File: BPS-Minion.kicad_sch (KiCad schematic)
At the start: 138 parts, among them J1 TopConn, J10 TempConn2, J11 SOMConnector, J2 BottomConn, J3 Conn_01x24_Female, J3 DTENConfig, J4 IsoConfig, J5 IN, J6 OUT, J8 RegularSPIConn, J9 TempConn1, Q1 BSS308PE, Q10 BSS308PE, Q11 BSS308PE, Q12 BSS308PE, Q13 NSV1C201MZ4, Q2 BSS308PE, Q3 BSS308PE, Q4 BSS308PE, Q5 BSS308PE, Q6 BSS308PE, Q7 BSS308PE, Q8 BSS308PE, Q9 BSS308PE, SW1 Power Switch, U1 ADS7953SBDBT, U1 LTC6811-1, U2 HX1188FNL, U3 LM321, U3 LTC6255, U4 LTC1380, U5 LTC1380

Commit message: ADC Power all 3.3V
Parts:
- removed C1, C10, C11, C12, C2, C3, C4, C5, C6, C7, C8, C9: 10n, Capacitor_SMD:C_0805_2012Metric, symbol Device:C_Small
- removed C13, C20: 100n, Capacitor_SMD:C_0805_2012Metric, symbol Device:C_Small
- removed C14, C15, C16: 1u, Capacitor_SMD:C_0805_2012Metric, symbol Device:C_Small
- removed L1, L10, L11, L12, L2, L3, L4, L5, L6, L7, L8, L9: 600, Inductor_SMD:L_0805_2012Metric, symbol Device:Ferrite_Bead_Small
- removed Q1, Q10, Q11, Q12, Q2, Q3, Q4, Q5, Q6, Q7, Q8, Q9: BSS308PE, Package_TO_SOT_SMD:SOT-23, symbol Device:Q_PMOS_GSD
- removed Q13: NSV1C201MZ4, Package_TO_SOT_SMD:SOT-223, symbol Device:Q_NPN_BCEC
- removed R1, R10, R11, R12, R2, R3, R4, R5, R6, R7, R8, R9: 33R, Resistor_SMD:R_2512_6332Metric, symbol Device:R_Small
- removed R13, R14, R15, R16, R17, R18, R19, R20, R21, R22, R23, R24, R25: 100, Resistor_SMD:R_0805_2012Metric, symbol Device:R_Small
- removed R26: 100, Resistor_SMD:R_0805_2012Metric, symbol Device:R
- removed R27: 806, Resistor_SMD:R_0805_2012Metric, symbol Device:R_Small
- removed R28: 1.2k, Resistor_SMD:R_0805_2012Metric, symbol Device:R_Small
- removed SW1: Power Switch, Button_Switch_THT:SW_CuK_OS102011MA1QN1_SPDT_Angled, symbol Switch:SW_SPDT
- removed TP1: V+, TestPoint:TestPoint_Keystone_5005-5009_Compact, symbol Connector:TestPoint
- removed TP2: VREG, TestPoint:TestPoint_Keystone_5005-5009_Compact, symbol Connector:TestPoint
- removed TP3: V-, TestPoint:TestPoint_Keystone_5005-5009_Compact, symbol Connector:TestPoint
- removed U1: LTC6811-1, UTSVT_BPS:LTC6811HG-1-PBF, symbol utsvt-bps:LTC6811-1
- added U4: BQ7695201PFBR, Package_QFP:TQFP-48_7x7mm_P0.5mm, symbol utsvt-chips:BQ7695201PFBR
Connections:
- net +3.3V: now also U1.4 (REFP), U1.5 (VA+)
- net +5V: no longer U1.29 (VA+), U1.4 (REFP), U1.5 (VA+)
- net GND: no longer D12.1 (K)
- new net Batt0: D12.1 (K)
- new net LDO1: U1.29 (VA+)
- no-connect marks 13 -> 9
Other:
- note removed: "These Jumpers are for configuring the board to measure less than 12 cells"
- note removed: "These capacitors should have a voltage rating greater than 50V"
- moved on the sheet: U1

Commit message: bms chip started
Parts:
- removed C17: 10n, Capacitor_SMD:C_0805_2012Metric, symbol Device:C_Small
- removed C18, C19: 100n, Capacitor_SMD:C_0805_2012Metric, symbol Device:C_Small
- removed J10: TempConn2, Connector_PinHeader_2.54mm:PinHeader_1x10_P2.54mm_Vertical, symbol Connector_Generic:Conn_01x10
- removed J9: TempConn1, Connector_PinHeader_2.54mm:PinHeader_1x10_P2.54mm_Vertical, symbol Connector_Generic:Conn_01x10
- removed R43: 100, Resistor_SMD:R_0805_2012Metric, symbol Device:R_Small
- removed R44, R46: 4.7k, Resistor_SMD:R_0805_2012Metric, symbol Device:R_Small
- removed R47: 10k, Resistor_SMD:R_0805_2012Metric, symbol Device:R_Small
- removed U3: LTC6255, UTSVT_BPS:LTC6255CS6-TRMPBF, symbol utsvt-bps:LTC6255
- removed U4, U5: LTC1380, UTSVT_BPS:LTC1380CS-PBF, symbol utsvt-bps:LTC1380
- added C1, C10, C11, C12, C13, C14, C15, C16, C2, C3, C4, C5, C6, C7, C8, C9: 220nF, symbol Device:C
- added R1, R10, R11, R12, R13, R14, R15, R16, R2, R3, R4, R5, R6, R7, R8, R9: 20, symbol Device:R_US
- J1, J2: symbol Connector_Generic:Conn_01x07 -> Connector_Generic:Conn_01x08
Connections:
- net +3.3V: now also U3.5 (V+); no longer U1.4 (REFP)
- net +5V: no longer U3.5 (V+)
- net GND: now also U4.16 (VC0), C16.1; no longer U1.3 (REFM)
- net GNDA: now also U1.3 (REFM)
- net VDDA: now also U1.4 (REFP)
- net at J2.1 (Pin_1): now also R16.2
- net at J2.2 (Pin_2): now also R15.2
- net at J2.3 (Pin_3): now also R14.2
- net at J2.4 (Pin_4): now also R13.2
- net at J2.5 (Pin_5): now also R12.2
- net at J2.6 (Pin_6): now also R11.2
- net at J2.7 (Pin_7): now also R10.2
- net at J1.1 (Pin_1): now also R8.2
- net at J1.2 (Pin_2): now also R7.2
- net at J1.3 (Pin_3): now also R6.2
- net at J1.4 (Pin_4): now also R5.2
- net at J1.5 (Pin_5): now also R4.2
- net at J1.6 (Pin_6): now also R3.2
- net at J1.7 (Pin_7): now also R2.2
- net cell15: now reaches U4.1 (VC15)
- net cell15: now also C1.1, C2.2, R2.1
- net cell6: now reaches U4.10 (VC6)
- net cell6: now also C10.1, C11.2, R11.1
- net cell5: now reaches U4.11 (VC5)
- net cell5: now also C11.1, C12.2, R12.1
- net cell4: now reaches U4.12 (VC4)
- net cell4: now also C12.1, C13.2, R13.1
- net cell3: now reaches U4.13 (VC3)
- net cell3: now also C13.1, C14.2, R14.1
- net cell2: now reaches U4.14 (VC2)
- net cell2: now also C14.1, C15.2, R15.1
- net cell1: now reaches U4.15 (VC1)
- net cell1: now also C15.1, C16.2, R16.1
- net cell14: now reaches U4.2 (VC14)
- net cell14: now also C2.1, C3.2, R3.1
- net cell13: now reaches U4.3 (VC13)
- net cell13: now also C3.1, C4.2, R4.1
- net cell12: now reaches U4.4 (VC12)
- net cell12: now also C4.1, C5.2, R5.1
- net cell16: now reaches U4.48 (VC16)
- net cell16: now also C1.2, R1.1
- net cell11: now reaches U4.5 (VC11)
- net cell11: now also C5.1, C6.2, R6.1
- net cell10: now reaches U4.6 (VC10)
- net cell10: now also C6.1, C7.2, R7.1
- net cell9: now reaches U4.7 (VC9)
- net cell9: now also C7.1, C8.2, R8.1
- net cell8: now reaches U4.8 (VC8)
- net cell8: now also C8.1, C9.2, R9.1
- net cell7: now reaches U4.9 (VC7)
- net cell7: now also C10.2, C9.1, R10.1
- new net: J2.8 (Pin_8), R9.2
- new net: J1.8 (Pin_8), R1.2
- no-connect marks 9 -> 8
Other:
- moved on the sheet: C21, C22, FB17, FB18, J11, J3, R49, R50, U1, U3, U4

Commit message: BMS chip is fully wired
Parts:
- removed J5: IN, Connector_Molex:Molex_Micro-Fit_3.0_43650-0200_1x02_P3.00mm_Horizontal, symbol Connector_Generic:Conn_01x02
- removed J6: OUT, Connector_Molex:Molex_Micro-Fit_3.0_43650-0200_1x02_P3.00mm_Horizontal, symbol Connector_Generic:Conn_01x02
- removed J8: RegularSPIConn, Connector_PinHeader_2.54mm:PinHeader_1x05_P2.54mm_Vertical, symbol Connector_Generic:Conn_01x05
- removed R29, R30: 120, Resistor_SMD:R_0805_2012Metric, symbol Device:R_Small
- removed R48: 5.1k, Resistor_SMD:R_0805_2012Metric, symbol Device:R_Small
- removed U2: HX1188FNL, UTSVT_Passive:HXXXX, symbol utsvt-chips:HX1188FNL
- added C17: 220nF, symbol Device:C
- added C18: 4.7u, symbol Device:C
- added C19: 1u, symbol Device:C
- added C20: 100p, symbol Device:C
- added D14: D, symbol Device:D
- added J6: TopConn, Connector_Molex:Molex_Micro-Fit_3.0_43650-0700_1x07_P3.00mm_Horizontal, symbol Connector_Generic:Conn_01x06
- added R17: 20, symbol Device:R_US
- added R18, R19: 10k, symbol Device:R_US
- added R20: 100, symbol Device:R_US
- added TP1, TP10, TP11, TP12, TP13, TP14, TP15, TP2, TP3, TP4, TP5, TP6, TP7, TP8, TP9: TestPoint_2Pole, symbol Connector:TestPoint_2Pole
- J1, J2: symbol Connector_Generic:Conn_01x08 -> Connector_Generic:Conn_01x06
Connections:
- net GND: now also J2.1 (Pin_1), U4.17 (VSS), U4.18 (SRP), U4.20 (SRN), U4.36 (REGIN), U4.37 (BREG), C17.1, C18.1, C19.1, C20.1, R17.2; no longer U4.16 (VC0)
- net I2C1_SCL: now also U4.26 (SCL)
- net I2C1_SDA: now also U4.27 (SDA)
- net SPI2_MISO: now also U4.32 (DDSG)
- net SPI2_MOSI: now also U4.31 (DCHG)
- net SPI2_NSS: now also U4.33 (RST_SHUT)
- net SPI2_SCK: now also U4.38 (FUSE)
- net cell1: now also TP15.1
- net cell10: now also TP6.1, TP7.2
- net cell11: now also TP5.1, TP6.2
- net cell12: now also TP4.1, TP5.2
- net cell13: now also TP3.1, TP4.2
- net cell14: now also TP2.1, TP3.2
- net cell15: now also TP1.1, TP2.2
- net cell16: now also TP1.2
- net cell2: now also TP14.1, TP15.2
- net cell3: now also TP13.1, TP14.2
- net cell4: now also TP12.1, TP13.2
- net cell5: now also TP11.1, TP12.2
- net cell6: now also TP10.1, TP11.2
- net cell7: now also TP10.2, TP9.1
- net cell8: now also TP8.1, TP9.2
- net cell9: now also TP7.1, TP8.2
- net at R16.2: now also J2.2 (Pin_2); no longer J2.1 (Pin_1)
- net at R15.2: now also J2.3 (Pin_3); no longer J2.2 (Pin_2)
- net at R14.2: now also J2.4 (Pin_4); no longer J2.3 (Pin_3)
- net at R13.2: now also J2.5 (Pin_5); no longer J2.4 (Pin_4)
- net at R12.2: now also J2.6 (Pin_6); no longer J2.5 (Pin_5)
- net at R11.2: now also J1.1 (Pin_1); no longer J2.6 (Pin_6)
- net at R10.2: now also J1.2 (Pin_2); no longer J2.7 (Pin_7)
- net at R9.2: now also J1.3 (Pin_3); no longer J2.8 (Pin_8)
- net at R8.2: now also J1.4 (Pin_4); no longer J1.1 (Pin_1)
- net at R7.2: now also J1.5 (Pin_5); no longer J1.2 (Pin_2)
- net at R6.2: now also J1.6 (Pin_6); no longer J1.3 (Pin_3)
- net at R5.2: now also J6.1 (Pin_1); no longer J1.4 (Pin_4)
- net at R4.2: now also J6.2 (Pin_2); no longer J1.5 (Pin_5)
- net at R3.2: now also J6.3 (Pin_3); no longer J1.6 (Pin_6)
- net at R2.2: now also J6.4 (Pin_4); no longer J1.7 (Pin_7)
- net PACK+: now reaches R1.2
- net PACK+: now also D14.2 (A), J6.5 (Pin_5), R18.1, R19.1; no longer J1.8 (Pin_8)
- net at U4.24 (REG18): now also C18.2
- net at U4.41 (LD): now also R19.2
- net at U4.42 (PACK): now also R18.2
- net at U4.46 (CP1): now also U4.47 (BAT), C19.2, C20.2, R20.1
- new net: D14.1 (K), R20.2
- new net cell0: C17.2, R17.1, U4.16 (VC0)
- no-connect marks 8 -> 17
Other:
- note removed: "SDO is an open-drain output so a pull-up resistor is required for regular SPI."
- moved on the sheet: C1, C10, C11, C12, C13, C14, C15, C16, C2, C3, C4, C5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

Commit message: clean up
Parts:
- removed D1, D10, D11, D12, D2, D3, D4, D5, D6, D7, D8, D9: Red, LED_SMD:LED_0805_2012Metric, symbol Device:LED
- removed J3: DTENConfig, Connector_PinHeader_2.54mm:PinHeader_1x03_P2.54mm_Vertical, symbol Connector_Generic:Conn_01x03
- removed J4: IsoConfig, Connector_PinHeader_2.54mm:PinHeader_1x03_P2.54mm_Vertical, symbol Connector_Generic:Conn_01x03
- removed R31, R32, R33, R34, R35, R36, R37, R38, R39, R40, R41, R42: 1.2k, Resistor_SMD:R_0805_2012Metric, symbol Device:R
- removed R45: 1.5k, Resistor_SMD:R_0805_2012Metric, symbol Device:R
- added C23, C25: 4.7u, symbol Device:C
- added C24: 1u, symbol Device:C
- added C26: .47u, symbol Device:C
- added R21: 1k, symbol Device:R_US
- added U2: REF35160QDBVR, Package_SO:TSOP-6_1.65x3.05mm_P0.95mm, symbol utsvt-power-regulators:REF35160QDBVR
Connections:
- net LDO1 is gone; now on net VDDA: U1.29 (VA+)
- net +3.3V: no longer U1.5 (VA+)
- net +5V: now also R21.2
- net GND: no longer U1.19 (AGND), U1.20 (AGND)
- net GNDA: now also U1.19 (AGND), U1.20 (AGND), C23.1, C24.2, C25.2, U2.1 (GND), U2.2 (GND)
- net VDDA: now also U1.5 (VA+), C23.2, U2.3 (EN), U2.4 (VIN); no longer U1.4 (REFP)
- net at D13.2 (A): now also R21.1
- net at C19.2, C20.2, R20.1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: now also C26.2; no longer U4.46 (CP1)
- new net: C26.1, U4.46 (CP1)
- new net: C24.1, U2.5 (NR)
- new net 2V5_Ref: C25.1, U1.4 (REFP), U2.6 (VREF)
- no-connect marks 17 -> 21
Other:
- note added: "BMS"
- note added: "SOM Connection Input"
- note added: "Temp Sensor Connector"
- note added: "Temperature ADC and Filter"
- moved on the sheet: C18, C19, C20, C21, C22, D13, D14, FB17, FB18, J11, J3, MH1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

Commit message: edited some mistakes out
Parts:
- removed D14: D, symbol Device:D
- added D1: BAS16W, Package_TO_SOT_SMD:SOT-323_SC-70, symbol Diode:BAS16W
- C1, C10, C11, C12, C13, C14, C15, C16, C17, C18, C19, C2, C20, C23, C24, C25, C26, C3, C4, C5, C6, C7, C8, C9: footprint (none) -> Capacitor_SMD:C_0805_2012Metric_Pad1.18x1.45mm_HandSolder
- C21, C22: value C -> 47n; footprint (none) -> Capacitor_SMD:C_0805_2012Metric_Pad1.18x1.45mm_HandSolder
- R1, R10, R11, R12, R13, R14, R15, R16, R17, R18, R19, R2, R20, R21, R3, R4, R5, R6, R7, R8, R9: footprint (none) -> Resistor_SMD:R_0805_2012Metric_Pad1.20x1.40mm_HandSolder
- R49, R50: value R_US -> 4.7k; footprint (none) -> Resistor_SMD:R_0805_2012Metric_Pad1.20x1.40mm_HandSolder
- TP1, TP10, TP11, TP12, TP13, TP14, TP15, TP2, TP3, TP4, TP5, TP6, TP7, TP8, TP9: footprint (none) -> Jumper:SolderJumper-2_P1.3mm_Open_RoundedPad1.0x1.5mm
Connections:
- net PACK+: now also D1.1 (A)
- net at R20.2: now also D1.3 (K)
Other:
- moved on the sheet: R20

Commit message: new sheets
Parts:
- removed C1, C10, C11, C12, C13, C14, C15, C16, C17, C2, C3, C4, C5, C6, C7, C8, C9: 220nF, Capacitor_SMD:C_0805_2012Metric_Pad1.18x1.45mm_HandSolder, symbol Device:C
- removed C18, C23, C25: 4.7u, Capacitor_SMD:C_0805_2012Metric_Pad1.18x1.45mm_HandSolder, symbol Device:C
- removed C19, C24: 1u, Capacitor_SMD:C_0805_2012Metric_Pad1.18x1.45mm_HandSolder, symbol Device:C
- removed C20: 100p, Capacitor_SMD:C_0805_2012Metric_Pad1.18x1.45mm_HandSolder, symbol Device:C
- removed C21, C22: 47n, Capacitor_SMD:C_0805_2012Metric_Pad1.18x1.45mm_HandSolder, symbol Device:C
- removed C26: .47u, Capacitor_SMD:C_0805_2012Metric_Pad1.18x1.45mm_HandSolder, symbol Device:C
- removed D1: BAS16W, Package_TO_SOT_SMD:SOT-323_SC-70, symbol Diode:BAS16W
- removed FB17, FB18: 2.2k, Inductor_SMD:L_0805_2012Metric_Pad1.05x1.20mm_HandSolder, symbol Device:FerriteBead_Small
- removed J1, J6: TopConn, Connector_Molex:Molex_Micro-Fit_3.0_43650-0700_1x07_P3.00mm_Horizontal, symbol Connector_Generic:Conn_01x06
- removed J2: BottomConn, Connector_Molex:Molex_Micro-Fit_3.0_43650-0700_1x07_P3.00mm_Horizontal, symbol Connector_Generic:Conn_01x06
- removed J3: Conn_01x24_Female, UTSVT_Connectors:PADP-24V-1-S, symbol Connector:Conn_01x24_Female
- removed R1, R10, R11, R12, R13, R14, R15, R16, R17, R2, R3, R4, R5, R6, R7, R8, R9: 20, Resistor_SMD:R_0805_2012Metric_Pad1.20x1.40mm_HandSolder, symbol Device:R_US
- removed R18, R19: 10k, Resistor_SMD:R_0805_2012Metric_Pad1.20x1.40mm_HandSolder, symbol Device:R_US
- removed R20: 100, Resistor_SMD:R_0805_2012Metric_Pad1.20x1.40mm_HandSolder, symbol Device:R_US
- removed R49, R50: 4.7k, Resistor_SMD:R_0805_2012Metric_Pad1.20x1.40mm_HandSolder, symbol Device:R_US
- removed TP1, TP10, TP11, TP12, TP13, TP14, TP15, TP2, TP3, TP4, TP5, TP6, TP7, TP8, TP9: TestPoint_2Pole, Jumper:SolderJumper-2_P1.3mm_Open_RoundedPad1.0x1.5mm, symbol Connector:TestPoint_2Pole
- removed U1: ADS7953SBDBT, Package_SO:HTSSOP-38-1EP_6.1x12.5mm_P0.65mm_EP5.2x12.5mm_Mask3.39x6.35mm, symbol utsvt-chips:ADS7953SBDBT
- removed U2: REF35160QDBVR, Package_SO:TSOP-6_1.65x3.05mm_P0.95mm, symbol utsvt-power-regulators:REF35160QDBVR
- removed U3: LM321, Package_TO_SOT_SMD:SOT-23-5, symbol Amplifier_Operational:LM321
- removed U4: BQ7695201PFBR, Package_QFP:TQFP-48_7x7mm_P0.5mm, symbol utsvt-chips:BQ7695201PFBR
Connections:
- no-connect marks 21 -> 0
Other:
- added sheet BMS (BMS.kicad_sch)
- added sheet Temperature (Temperature.kicad_sch)
- note removed: "BMS"
- note removed: "Temp Sensor Connector"
- note removed: "Temperature ADC and Filter"

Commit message: main sheet fixes
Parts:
- removed J11: SOMConnector, UTSVT_Connectors:Molex_52465-2070, symbol utsvt-connectors:SOMConnector
- added J5: SOMConnector, UTSVT_Connectors:Molex_52465-2070, symbol utsvt-connectors:SOMConnector
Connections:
- net +5V is gone; now on net +3.3V: R21.2
- net +3.3V: now also J5.2, J5.9
- net GND: now also J5.11, J5.4
- net GNDA: now also J5.12
- net I2C1_SCL: now also J5.14
- net I2C1_SDA: now also J5.16
- net I2C2_SCL: now also J5.8
- net I2C2_SDA: now also J5.6
- net SPI1_MISO: now also J5.15
- net SPI1_MOSI: now also J5.17
- net SPI1_NSS: now also J5.19
- net SPI1_SCK: now also J5.13
- net SPI2_MISO: now also J5.3
- net SPI2_MOSI: now also J5.1
- net SPI2_NSS: now also J5.7
- net SPI2_SCK: now also J5.5
- net VDDA: now also J5.10
- new net PA1: J5.20
- new net PA2: J5.18
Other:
- added sheet Temperature1 (Temperature.kicad_sch)
- moved on the sheet: D13, R21

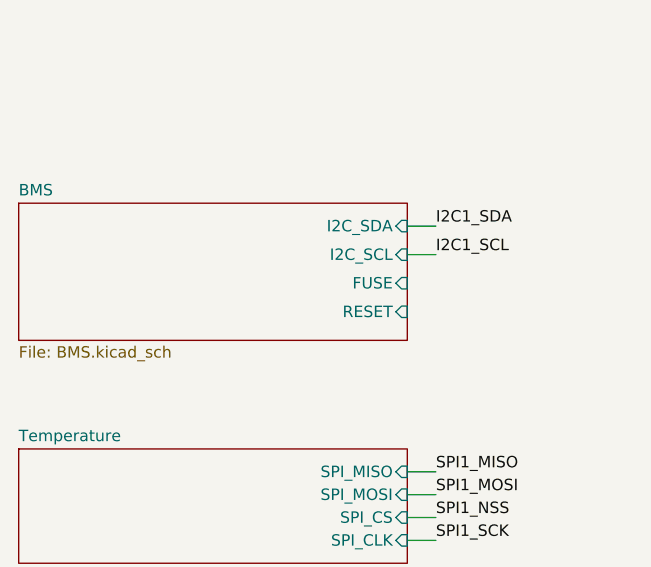
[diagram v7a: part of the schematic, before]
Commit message: stacked bms schematic
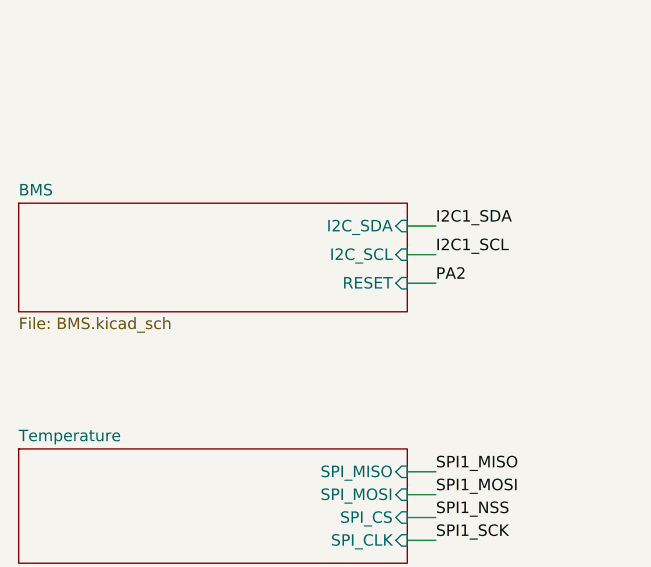
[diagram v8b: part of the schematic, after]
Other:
- sheet BMS ports: added none; removed FUSE
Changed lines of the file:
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@@
+    (stroke (width 0) (type default))
+  )
+  (wire (pts (xy 80.645 76.2) (xy 83.82 76.2))
     (stroke (width 0) (type default))
   )
@@
   )
   (label "I2C1_SCL" (at 83.82 73.025 0) (fields_autoplaced)
+    (effects (font (size 1.27 1.27)) (justify left bottom))
+  )
+  (label "PA2" (at 83.82 76.2 0) (fields_autoplaced)
     (effects (font (size 1.27 1.27)) (justify left bottom))
   )
@@
     )
   )
-  (sheet (at 37.465 67.31) (size 43.18 15.24) (fields_autoplaced)
+  (sheet (at 37.465 67.31) (size 43.18 12.065) (fields_autoplaced)
     (stroke (width 0.1524) (type solid))
     (fill (color 0 0 0 0.0000))
@@
       (effects (font (size 1.27 1.27)) (justify left bottom))
     )
-    (property "Sheetfile" "BMS.kicad_sch" (at 37.465 83.1346 0)
+    (property "Sheetfile" "BMS.kicad_sch" (at 37.465 79.9596 0)
       (effects (font (size 1.27 1.27)) (justify left top))
     )
-    (pin "RESET" input (at 80.645 79.375 0)
-      (effects (font (size 1.27 1.27)) (justify right))
-    )
-    (pin "FUSE" input (at 80.645 76.2 0)
-      (effects (font (size 1.27 1.27)) (justify right))
-    )
+    (pin "RESET" input (at 80.645 76.2 0)
+      (effects (font (size 1.27 1.27)) (justify right))
+    )
